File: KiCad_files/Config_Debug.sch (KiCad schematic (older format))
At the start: 50 parts, among them J3 Conn_01x06, J4 USB_C_Receptacle, SW1 SW_Push, U1 XC7A35T_CSG325, U10 W25Q128JV, U6 FT2232HL, U7 93LCxxC, U8 SiT8209, U9 SiT9102, Y1 12MHz

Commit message: Cleanup + Update to KiCad 5.0 + DDR2
Updated to KiCad 5, which re-organized libraries, so corrected them to not need RASAC-rescue.lib.
Also cleaned up some stuff.
DDR4 has been removed and in place will be DDR2.
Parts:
- C69, C70, C71, C72, C73, C74, C75, C76, C77, C78, C79, C80, C81: symbol C_Small -> Device:C_Small
- C82, C83, C84, C85: symbol C -> Device:C
- D3, D4: symbol LED -> Device:LED
- J3: symbol Conn_01x06 -> Connector_Generic:Conn_01x06
- J4: symbol USB_C_Receptacle -> Connector:USB_C_Receptacle_USB2.0
- L4, L5: symbol L_Core_Iron -> Device:L_Core_Iron
- R10, R11, R12, R13, R14, R15, R16, R17, R18, R19, R20, R21, R22, R23, R24, R25, R7, R8, R9: symbol R -> Device:R
- SW1: symbol SW_Push -> Switch:SW_Push
- U1: symbol XC7A35T_CSG325 -> custom:XC7A35T_CSG325
- U10: symbol W25Q128JV -> custom:W25Q128JV
- U6: symbol FT2232HL -> custom:FT2232HL
- U7: symbol 93LCxxC -> Memory_EEPROM:93LCxxC
- U8: symbol SiT8209 -> custom:SiT8209
- U9: symbol SiT9102 -> custom:SiT9102
- Y1: symbol Crystal -> Device:Crystal
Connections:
- wire segments 170 -> 229
- no-connect marks 17 -> 9

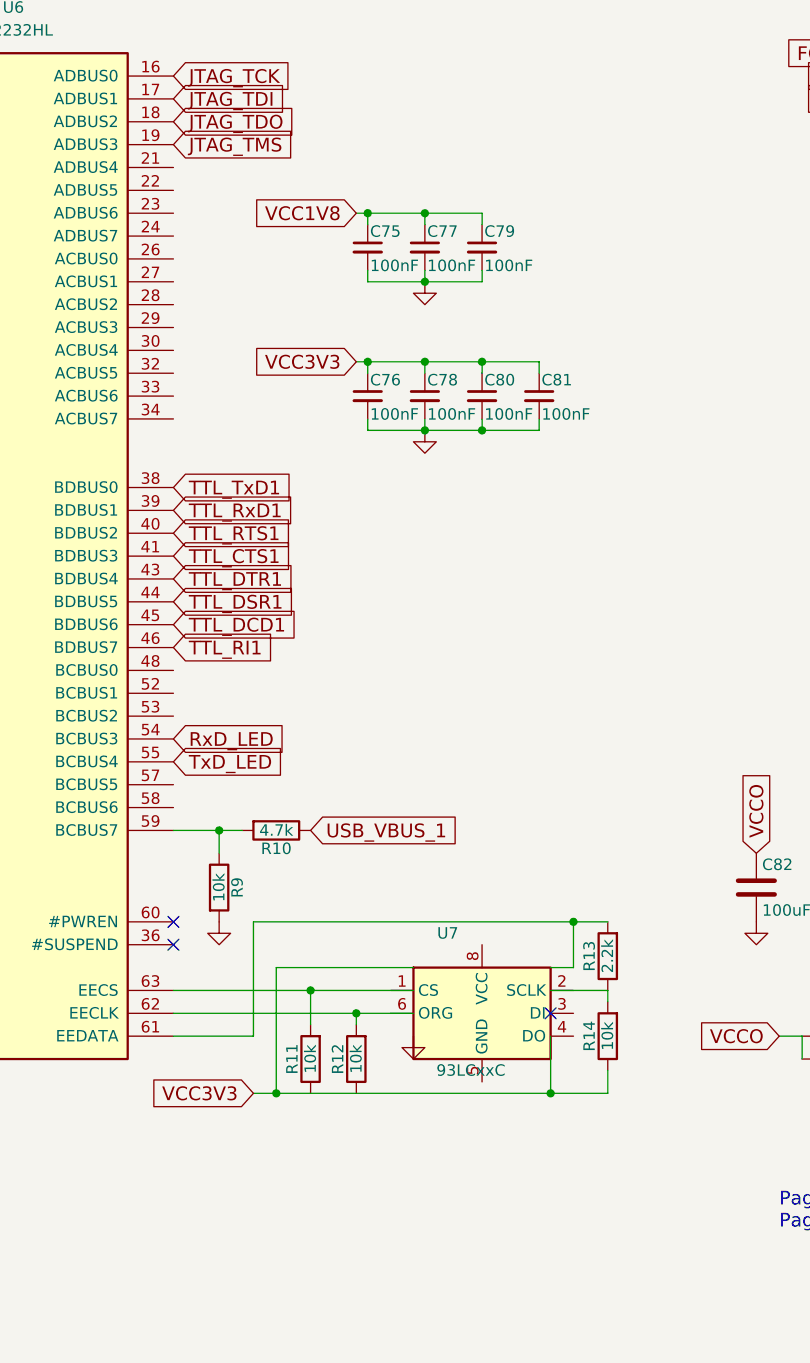
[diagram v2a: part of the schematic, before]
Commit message: Minor fixes
Still fixing from KiCad update
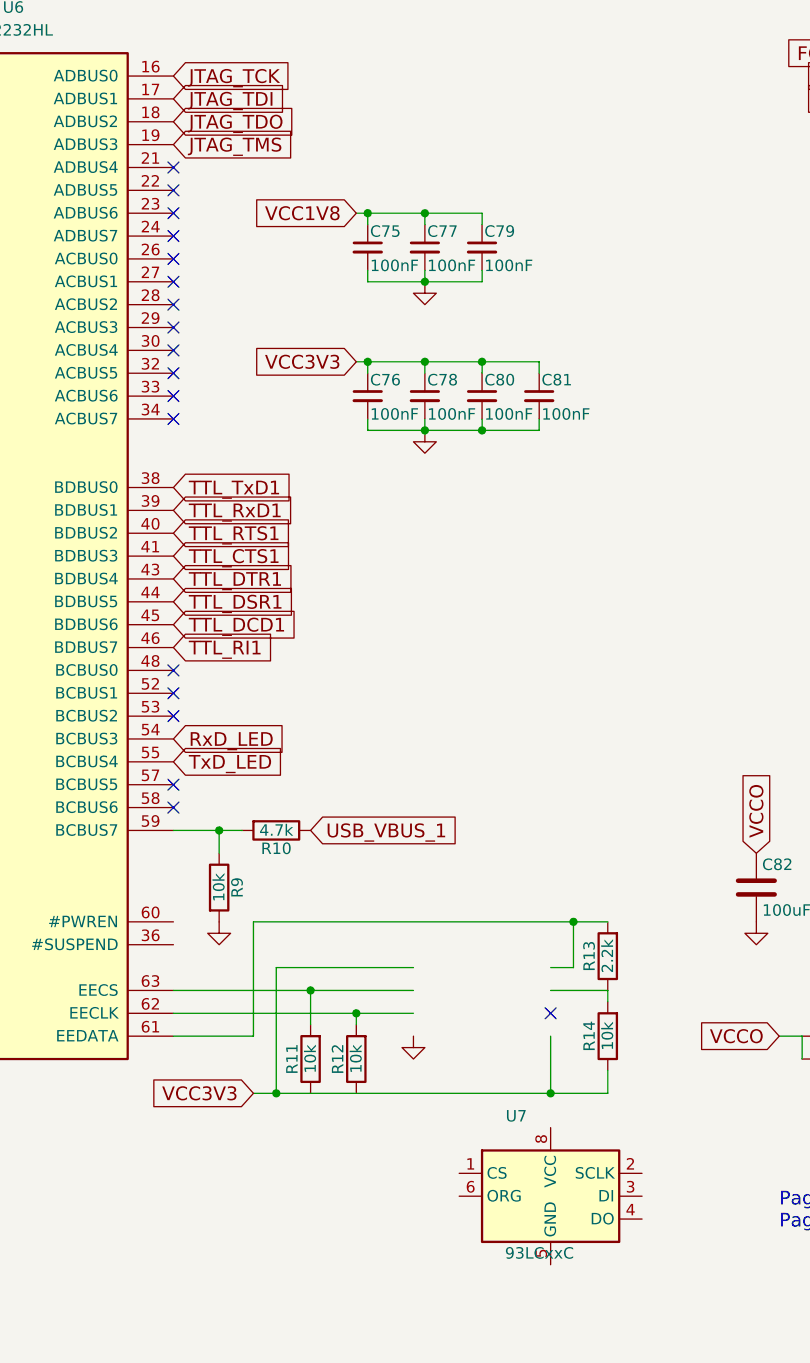
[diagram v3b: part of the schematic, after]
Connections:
- no-connect marks 9 -> 24
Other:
- moved on the sheet: U7
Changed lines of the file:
@@
 	1    0    0    -1
 $EndComp
-NoConn ~ 4850 5000
-NoConn ~ 4850 5100
 Text GLabel 1800 1800 0    60   Input ~ 0
 VCC3V3
@@
 L Memory_EEPROM:93LCxxC U7
 U 1 1 5C194DEC
-P 6200 5400
+P 6500 6200
 AR Path="/5C194DEC" Ref="U7"  Part="1"
 AR Path="/5C0630AC/5C194DEC" Ref="U7"  Part="1"
-F 0 "U7" H 6050 5750 50  0000 C CNN
-F 1 "93LCxxC" H 6000 5150 50  0000 L CNN
-F 2 "" H 6100 5400 50  0001 C CNN
-F 3 "" H 6200 5500 50  0001 C CNN
-	1    6200 5400
+F 0 "U7" H 6350 6550 50  0000 C CNN
+F 1 "93LCxxC" H 6300 5950 50  0000 L CNN
+F 2 "" H 6400 6200 50  0001 C CNN
+F 3 "" H 6500 6300 50  0001 C CNN
+	1    6500 6200
 	1    0    0    -1
 $EndComp
@@
 Wire Wire Line
 	1800 5050 2000 5050
+NoConn ~ 4850 1700
+NoConn ~ 4850 1800
+NoConn ~ 4850 1900
+NoConn ~ 4850 2000
+NoConn ~ 4850 2100
+NoConn ~ 4850 2200
+NoConn ~ 4850 2300
+NoConn ~ 4850 2400
+NoConn ~ 4850 2500
+NoConn ~ 4850 2600
+NoConn ~ 4850 2700
+NoConn ~ 4850 2800
+NoConn ~ 4850 3900
+NoConn ~ 4850 4000
+NoConn ~ 4850 4100
+NoConn ~ 4850 4400
+NoConn ~ 4850 4500
 $EndSCHEMATC

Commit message: More fixes
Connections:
- wire segments 229 -> 232
- no-connect marks 24 -> 23
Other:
- moved on the sheet: R11, R12, R13, R14, U7
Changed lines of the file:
@@
 L Memory_EEPROM:93LCxxC U7
 U 1 1 5C194DEC
-P 6500 6200
+P 5950 5400
 AR Path="/5C194DEC" Ref="U7"  Part="1"
 AR Path="/5C0630AC/5C194DEC" Ref="U7"  Part="1"
-F 0 "U7" H 6350 6550 50  0000 C CNN
-F 1 "93LCxxC" H 6300 5950 50  0000 L CNN
-F 2 "" H 6400 6200 50  0001 C CNN
-F 3 "" H 6500 6300 50  0001 C CNN
-	1    6500 6200
+F 0 "U7" H 5800 5750 50  0000 C CNN
+F 1 "93LCxxC" H 5750 5150 50  0000 L CNN
+F 2 "" H 5850 5400 50  0001 C CNN
+F 3 "" H 5950 5500 50  0001 C CNN
+	1    5950 5400
 	1    0    0    -1
 $EndComp
@@
 L Device:R R13
 U 1 1 5C194DF3
-P 6750 5150
-F 0 "R13" V 6830 5150 50  0000 C CNN
-F 1 "2.2k" V 6750 5150 50  0000 C CNN
-F 2 "" V 6680 5150 50  0001 C CNN
-F 3 "" H 6750 5150 50  0001 C CNN
-	1    6750 5150
-	-1   0    0    1
-$EndComp
-Text GLabel 5200 5750 0    60   Input ~ 0
+P 6500 5500
+F 0 "R13" V 6580 5500 50  0000 C CNN
+F 1 "2.2k" V 6500 5500 50  0000 C CNN
+F 2 "" V 6430 5500 50  0001 C CNN
+F 3 "" H 6500 5500 50  0001 C CNN
+	1    6500 5500
+	0    -1   -1   0
+$EndComp
+Text GLabel 6050 4900 2    60   Input ~ 0
 VCC3V3
 $Comp
 L Device:R R12
 U 1 1 5C194DFB
-P 5650 5600
-F 0 "R12" V 5730 5600 50  0000 C CNN
-F 1 "10k" V 5650 5600 50  0000 C CNN
-F 2 "" V 5580 5600 50  0001 C CNN
-F 3 "" H 5650 5600 50  0001 C CNN
-	1    5650 5600
+P 6450 5150
+F 0 "R12" V 6530 5150 50  0000 C CNN
+F 1 "10k" V 6450 5150 50  0000 C CNN
+F 2 "" V 6380 5150 50  0001 C CNN
+F 3 "" H 6450 5150 50  0001 C CNN
+	1    6450 5150
 	-1   0    0    1
 $EndComp
@@
 L Device:R R11
 U 1 1 5C194E02
-P 5450 5600
-F 0 "R11" V 5530 5600 50  0000 C CNN
-F 1 "10k" V 5450 5600 50  0000 C CNN
-F 2 "" V 5380 5600 50  0001 C CNN
-F 3 "" H 5450 5600 50  0001 C CNN
-	1    5450 5600
+P 5350 5150
+F 0 "R11" V 5430 5150 50  0000 C CNN
+F 1 "10k" V 5350 5150 50  0000 C CNN
+F 2 "" V 5280 5150 50  0001 C CNN
+F 3 "" H 5350 5150 50  0001 C CNN
+	1    5350 5150
 	-1   0    0    1
 $EndComp
@@
 L Device:R R14
 U 1 1 5C194E09
-P 6750 5500
-F 0 "R14" V 6830 5500 50  0000 C CNN
-F 1 "10k" V 6750 5500 50  0000 C CNN
-F 2 "" V 6680 5500 50  0001 C CNN
-F 3 "" H 6750 5500 50  0001 C CNN
-	1    6750 5500
+P 6650 5150
+F 0 "R14" V 6730 5150 50  0000 C CNN
+F 1 "10k" V 6650 5150 50  0000 C CNN
+F 2 "" V 6580 5150 50  0001 C CNN
+F 3 "" H 6650 5150 50  0001 C CNN
+	1    6650 5150
 	-1   0    0    1
 $EndComp
@@
 	6450 2850 6450 2800
 Connection ~ 6200 2850
-Wire Wire Line
-	4850 5300 5450 5300
-Wire Wire Line
-	4850 5400 5650 5400
-Wire Wire Line
-	6500 5200 6600 5200
-Wire Wire Line
-	6600 5200 6600 5000
-Wire Wire Line
-	5200 5000 6600 5000
-Wire Wire Line
-	5200 5000 5200 5500
-Wire Wire Line
-	5200 5500 4850 5500
-Connection ~ 6600 5000
-Wire Wire Line
-	6500 5300 6750 5300
-Wire Wire Line
-	5900 5200 5300 5200
-Wire Wire Line
-	5300 5200 5300 5750
-Wire Wire Line
-	5200 5750 5300 5750
-Wire Wire Line
-	5650 5450 5650 5400
-Connection ~ 5650 5400
-Wire Wire Line
-	5450 5300 5450 5450
-Connection ~ 5450 5300
-Connection ~ 5300 5750
-Wire Wire Line
-	6500 5750 6500 5500
-Connection ~ 6500 5750
-NoConn ~ 6500 5400
-Wire Wire Line
-	6750 5300 6750 5350
-Wire Wire Line
-	6750 5750 6750 5650
 $Comp
 L power:GND #PWR079
 U 1 1 5C194EA2
-P 5900 5500
-F 0 "#PWR079" H 5900 5250 50  0001 C CNN
-F 1 "GND" H 5900 5350 50  0001 C CNN
-F 2 "" H 5900 5500 50  0001 C CNN
-F 3 "" H 5900 5500 50  0001 C CNN
-	1    5900 5500
+P 5950 5700
+F 0 "#PWR079" H 5950 5450 50  0001 C CNN
+F 1 "GND" H 5950 5550 50  0001 C CNN
+F 2 "" H 5950 5700 50  0001 C CNN
+F 3 "" H 5950 5700 50  0001 C CNN
+	1    5950 5700
 	1    0    0    -1
 $EndComp
@@
 Wire Wire Line
 	6200 2850 6450 2850
-Wire Wire Line
-	6600 5000 6750 5000
-Wire Wire Line
-	5650 5400 5900 5400
-Wire Wire Line
-	5450 5300 5900 5300
-Wire Wire Line
-	5300 5750 6500 5750
-Wire Wire Line
-	6500 5750 6750 5750
 $Comp
 L Connector:USB_C_Receptacle_USB2.0 J4
@@
 NoConn ~ 4850 4400
 NoConn ~ 4850 4500
+Wire Wire Line
+	5950 5000 5500 5000
+Wire Wire Line
+	5500 5400 5550 5400
+Connection ~ 5950 5000
+Wire Wire Line
+	5550 5300 5350 5300
+Wire Wire Line
+	4850 5400 5400 5400
+Wire Wire Line
+	5400 5400 5400 5850
+Wire Wire Line
+	5400 5850 6450 5850
+Wire Wire Line
+	6450 5850 6450 5300
+Wire Wire Line
+	6450 5300 6350 5300
+Wire Wire Line
+	6300 5400 6350 5400
+Wire Wire Line
+	6650 5400 6650 5500
+Wire Wire Line
+	6650 5950 5300 5950
+Wire Wire Line
+	5300 5950 5300 5500
+Wire Wire Line
+	5300 5500 4850 5500
+Connection ~ 5350 5300
+Wire Wire Line
+	5350 5300 4850 5300
+Wire Wire Line
+	5500 5000 5500 5400
+Wire Wire Line
+	5950 5000 5950 5100
+Wire Wire Line
+	5500 5000 5350 5000
+Connection ~ 5500 5000
+Connection ~ 6450 5300
+Wire Wire Line
+	6650 5300 6650 5400
+Connection ~ 6650 5400
+Connection ~ 6450 5000
+Wire Wire Line
+	6050 4900 5950 4900
+Wire Wire Line
+	5950 4900 5950 5000
+Connection ~ 6350 5400
+Wire Wire Line
+	6350 5400 6650 5400
+Connection ~ 6650 5500
+Wire Wire Line
+	6650 5500 6650 5950
+Wire Wire Line
+	6450 5000 6650 5000
+Wire Wire Line
+	5950 5000 6450 5000
 $EndSCHEMATC

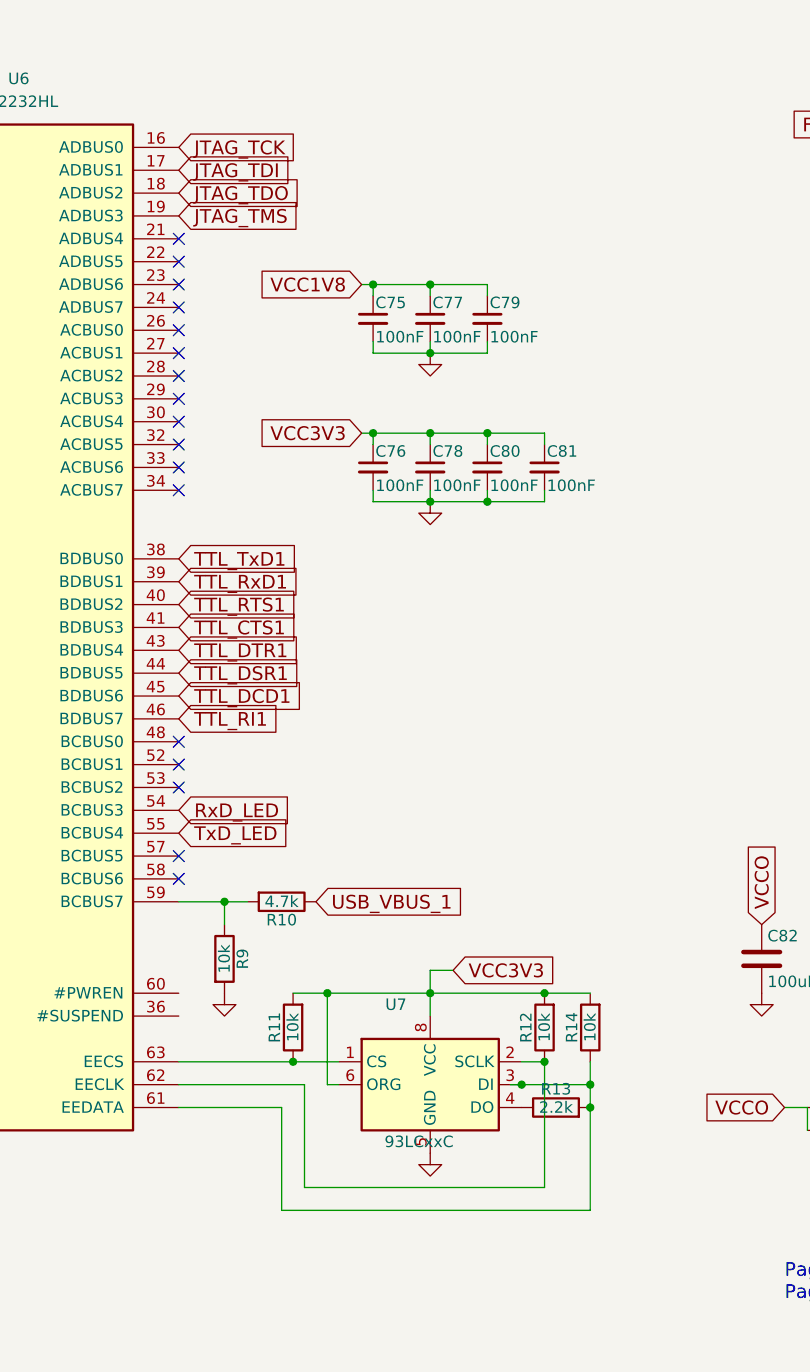
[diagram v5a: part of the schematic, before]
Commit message: Config_Debug and PCIe sheets look done
Added jumpers to JTAG chain.
Placed NCs on not used pins.
PCIe_PRSNT_B should be connected to the furthest PCIe_PRSNT_#.
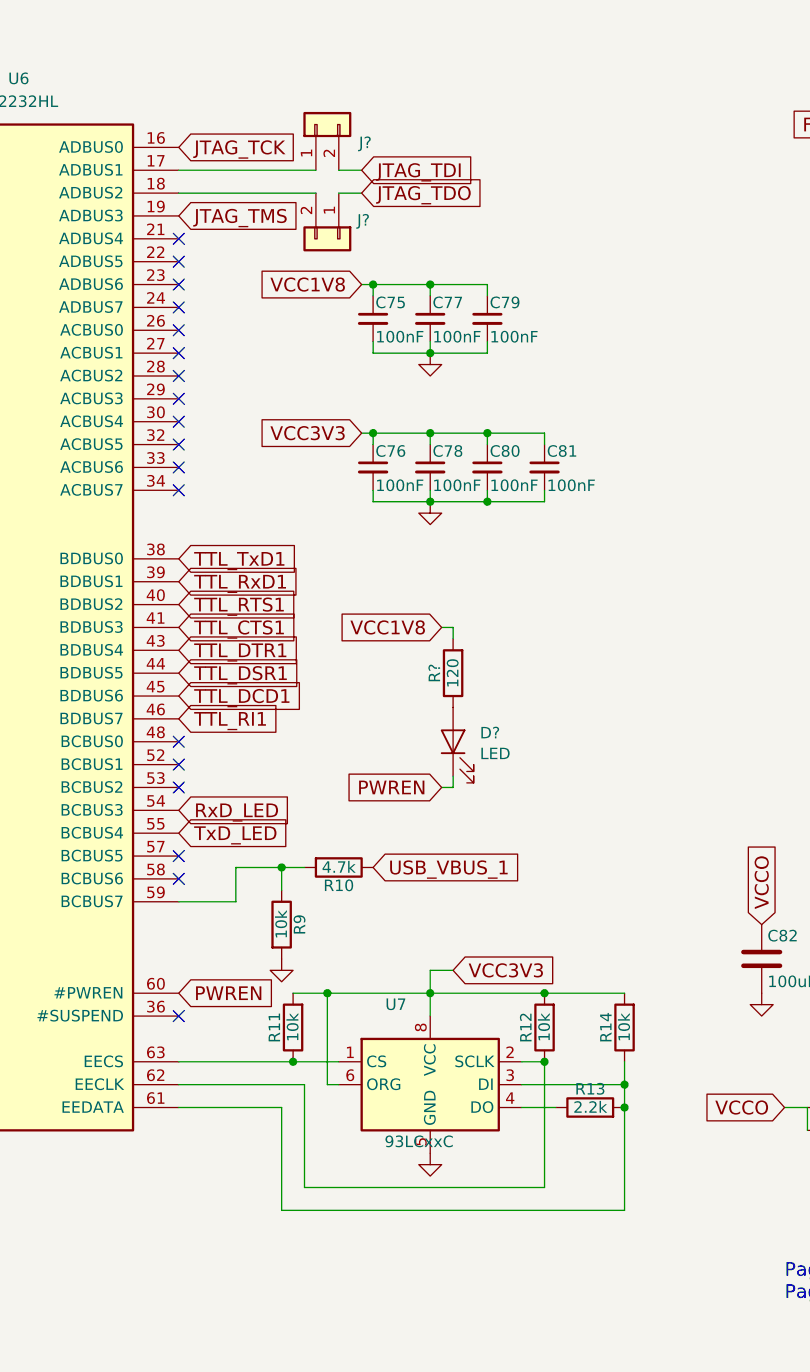
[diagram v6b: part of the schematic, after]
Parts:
- added D?: LED, symbol Device:LED
- added J? (x2): Conn_01x02, symbol Connector_Generic:Conn_01x02
- added R?: 120, symbol Device:R
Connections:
- net JTAG_TDI: now also J?.2 (Pin_2); no longer U6.17 (ADBUS1)
- net JTAG_TDO: now also J?.1 (Pin_1); no longer U6.18 (ADBUS2)
- net VCC1V8: now also R?.2
- net PWREN: now reaches U6.60 (#PWREN)
- net PWREN: now also D?.1 (K)
- new net: J?.1 (Pin_1), U6.17 (ADBUS1)
- new net: J?.2 (Pin_2), U6.18 (ADBUS2)
- new net: D?.2 (A), R?.1
- no-connect marks 23 -> 24
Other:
- moved on the sheet: R10, R13, R14, R9
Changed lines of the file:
@@
 Text GLabel 4850 1600 2    60   Input ~ 0
 JTAG_TMS
-Text GLabel 4850 1400 2    60   Input ~ 0
+Text GLabel 5650 1400 2    60   Input ~ 0
 JTAG_TDI
-Text GLabel 4850 1500 2    60   Input ~ 0
+Text GLabel 5650 1500 2    60   Input ~ 0
 JTAG_TDO
-Text GLabel 5450 4600 2    60   Input ~ 0
+Text GLabel 5700 4450 2    60   Input ~ 0
 USB_VBUS_1
 $Comp
 L Device:R R10
 U 1 1 5C194D66
-P 5300 4600
-F 0 "R10" V 5380 4600 50  0000 C CNN
-F 1 "4.7k" V 5300 4600 50  0000 C CNN
-F 2 "" V 5230 4600 50  0001 C CNN
-F 3 "" H 5300 4600 50  0001 C CNN
-	1    5300 4600
+P 5550 4450
+F 0 "R10" V 5630 4450 50  0000 C CNN
+F 1 "4.7k" V 5550 4450 50  0000 C CNN
+F 2 "" V 5480 4450 50  0001 C CNN
+F 3 "" H 5550 4450 50  0001 C CNN
+	1    5550 4450
 	0    1    1    0
 $EndComp
@@
 L Device:R R9
 U 1 1 5C194D6D
-P 5050 4850
-F 0 "R9" V 5130 4850 50  0000 C CNN
-F 1 "10k" V 5050 4850 50  0000 C CNN
-F 2 "" V 4980 4850 50  0001 C CNN
-F 3 "" H 5050 4850 50  0001 C CNN
-	1    5050 4850
+P 5300 4700
+F 0 "R9" V 5380 4700 50  0000 C CNN
+F 1 "10k" V 5300 4700 50  0000 C CNN
+F 2 "" V 5230 4700 50  0001 C CNN
+F 3 "" H 5300 4700 50  0001 C CNN
+	1    5300 4700
 	1    0    0    -1
 $EndComp
@@
 L power:GND #PWR078
 U 1 1 5C194D74
-P 5050 5000
-F 0 "#PWR078" H 5050 4750 50  0001 C CNN
-F 1 "GND" H 5050 4850 50  0001 C CNN
-F 2 "" H 5050 5000 50  0001 C CNN
-F 3 "" H 5050 5000 50  0001 C CNN
-	1    5050 5000
+P 5300 4850
+F 0 "#PWR078" H 5300 4600 50  0001 C CNN
+F 1 "GND" H 5300 4700 50  0001 C CNN
+F 2 "" H 5300 4850 50  0001 C CNN
+F 3 "" H 5300 4850 50  0001 C CNN
+	1    5300 4850
 	1    0    0    -1
 $EndComp
@@
 L Device:R R13
 U 1 1 5C194DF3
-P 6500 5500
-F 0 "R13" V 6580 5500 50  0000 C CNN
-F 1 "2.2k" V 6500 5500 50  0000 C CNN
-F 2 "" V 6430 5500 50  0001 C CNN
-F 3 "" H 6500 5500 50  0001 C CNN
-	1    6500 5500
+P 6650 5500
+F 0 "R13" V 6730 5500 50  0000 C CNN
+F 1 "2.2k" V 6650 5500 50  0000 C CNN
+F 2 "" V 6580 5500 50  0001 C CNN
+F 3 "" H 6650 5500 50  0001 C CNN
+	1    6650 5500
 	0    -1   -1   0
 $EndComp
@@
 L Device:R R14
 U 1 1 5C194E09
-P 6650 5150
-F 0 "R14" V 6730 5150 50  0000 C CNN
-F 1 "10k" V 6650 5150 50  0000 C CNN
-F 2 "" V 6580 5150 50  0001 C CNN
-F 3 "" H 6650 5150 50  0001 C CNN
-	1    6650 5150
+P 6800 5150
+F 0 "R14" V 6880 5150 50  0000 C CNN
+F 1 "10k" V 6800 5150 50  0000 C CNN
+F 2 "" V 6730 5150 50  0001 C CNN
+F 3 "" H 6800 5150 50  0001 C CNN
+	1    6800 5150
 	-1   0    0    1
 $EndComp
@@
 	2800 3400 2800 3000
 Wire Wire Line
-	4850 4600 5050 4600
-Wire Wire Line
-	5050 4600 5050 4700
-Connection ~ 5050 4600
+	5300 4450 5300 4550
 Wire Wire Line
 	1800 1800 1900 1800
@@
 	3400 3000 3450 3000
 Wire Wire Line
-	5050 4600 5150 4600
+	5300 4450 5400 4450
 Wire Wire Line
 	2400 1800 2900 1800
@@
 	6450 5300 6350 5300
 Wire Wire Line
-	6300 5400 6350 5400
-Wire Wire Line
-	6650 5400 6650 5500
-Wire Wire Line
-	6650 5950 5300 5950
+	6800 5950 5300 5950
 Wire Wire Line
 	5300 5950 5300 5500
@@
 Connection ~ 5500 5000
 Connection ~ 6450 5300
-Wire Wire Line
-	6650 5300 6650 5400
-Connection ~ 6650 5400
 Connection ~ 6450 5000
 Wire Wire Line
@@
 Wire Wire Line
 	5950 4900 5950 5000
-Connection ~ 6350 5400
-Wire Wire Line
-	6350 5400 6650 5400
-Connection ~ 6650 5500
-Wire Wire Line
-	6650 5500 6650 5950
-Wire Wire Line
-	6450 5000 6650 5000
+Connection ~ 6800 5500
+Wire Wire Line
+	6800 5500 6800 5950
+Wire Wire Line
+	6450 5000 6800 5000
 Wire Wire Line
 	5950 5000 6450 5000
+Wire Wire Line
+	6800 5300 6800 5400
+Wire Wire Line
+	6500 5500 6350 5500
+Wire Wire Line
+	6350 5400 6800 5400
+Connection ~ 6800 5400
+Wire Wire Line
+	6800 5400 6800 5500
+$Comp
+L Device:LED D?
+U 1 1 5C7C445B
+P 6050 3900
+F 0 "D?" V 6088 3783 50  0000 R CNN
+F 1 "LED" V 5997 3783 50  0000 R CNN
+F 2 "" H 6050 3900 50  0001 C CNN
+F 3 "~" H 6050 3900 50  0001 C CNN
+	1    6050 3900
+	0    -1   -1   0
+$EndComp
+$Comp
+L Device:R R?
+U 1 1 5C7C45F5
+P 6050 3600
+F 0 "R?" V 6130 3600 50  0000 C CNN
+F 1 "120" V 6050 3600 50  0000 C CNN
+F 2 "" V 5980 3600 50  0001 C CNN
+F 3 "" H 6050 3600 50  0001 C CNN
+	1    6050 3600
+	-1   0    0    1
+$EndComp
+Text GLabel 6000 3400 0    60   Input ~ 0
+VCC1V8
+Wire Wire Line
+	6000 3400 6050 3400
+Wire Wire Line
+	6050 3400 6050 3450
+Text GLabel 4850 5000 2    60   Input ~ 0
+PWREN
+Text GLabel 6000 4100 0    60   Input ~ 0
+PWREN
+Wire Wire Line
+	6000 4100 6050 4100
+Wire Wire Line
+	6050 4100 6050 4050
+Wire Wire Line
+	4850 4600 5100 4600
+Wire Wire Line
+	5100 4600 5100 4450
+Wire Wire Line
+	5100 4450 5300 4450
+Connection ~ 5300 4450
+NoConn ~ 4850 5100
+$Comp
+L Connector_Generic:Conn_01x02 J?
+U 1 1 5C82FBE2
+P 5550 1700
+F 0 "J?" V 5469 1780 50  0000 L CNN
+F 1 "Conn_01x02" H 5630 1601 50  0001 L CNN
+F 2 "" H 5550 1700 50  0001 C CNN
+F 3 "~" H 5550 1700 50  0001 C CNN
+	1    5550 1700
+	0    1    1    0
+$EndComp
+$Comp
+L Connector_Generic:Conn_01x02 J?
+U 1 1 5C82FC7A
+P 5450 1200
+F 0 "J?" V 5370 1012 50  0000 R CNN
+F 1 "Conn_01x02" H 5530 1101 50  0001 L CNN
+F 2 "" H 5450 1200 50  0001 C CNN
+F 3 "~" H 5450 1200 50  0001 C CNN
+	1    5450 1200
+	0    -1   -1   0
+$EndComp
+Wire Wire Line
+	4850 1400 5450 1400
+Wire Wire Line
+	5550 1400 5650 1400
+Wire Wire Line
+	5650 1500 5550 1500
+Wire Wire Line
+	5450 1500 4850 1500
 $EndSCHEMATC
